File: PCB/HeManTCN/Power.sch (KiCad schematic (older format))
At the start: 10 parts

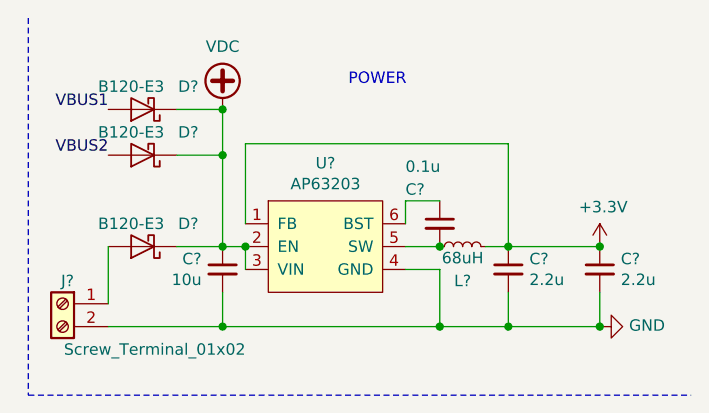
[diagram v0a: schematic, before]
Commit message: Hoja A1
Desarme las hojas jerarquicas y configure la hoja del esquematico como A1. Hay lugar suficiente (por ahora) para todo.
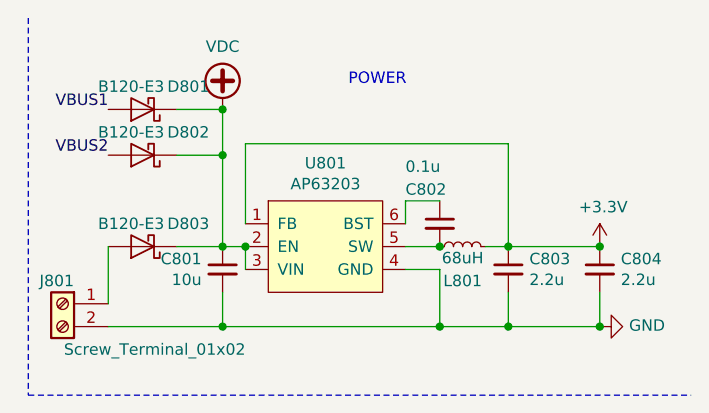
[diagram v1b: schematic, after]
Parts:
- gave numbers to parts that had none: 10
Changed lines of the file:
@@
 $Descr A4 11693 8268
 encoding utf-8
-Sheet 8 11
+Sheet 8 5
 Title "SnifferTCN"
 Date "2019-09-25"
@@
 U 1 1 5DA5E508
 P 6600 3850
-F 0 "C?" H 6692 3896 50  0000 L CNN
+AR Path="/5DA5E508" Ref="C?"  Part="1"
+AR Path="/5DA5E268/5DA5E508" Ref="C804"  Part="1"
+F 0 "C804" H 6692 3896 50  0000 L CNN
 F 1 "2.2u" H 6692 3805 50  0000 L CNN
 F 2 "Capacitor_SMD:C_0805_2012Metric" H 6600 3850 50  0001 C CNN
@@
 U 1 1 5DA5E510
 P 5900 3650
-F 0 "C?" H 5750 3800 50  0000 L CNN
+AR Path="/5DA5E510" Ref="C?"  Part="1"
+AR Path="/5DA5E268/5DA5E510" Ref="C802"  Part="1"
+F 0 "C802" H 5750 3800 50  0000 L CNN
 F 1 "0.1u" H 5750 3900 50  0000 L CNN
 F 2 "Capacitor_SMD:C_0805_2012Metric" H 5900 3650 50  0001 C CNN
@@
 U 1 1 5DA5E517
 P 6600 3750
-F 0 "#PWR?" H 6600 3600 50  0001 C CNN
+AR Path="/5DA5E517" Ref="#PWR?"  Part="1"
+AR Path="/5DA5E268/5DA5E517" Ref="#PWR0802"  Part="1"
+F 0 "#PWR0802" H 6600 3600 50  0001 C CNN
 F 1 "+3.3V" H 6615 3923 50  0000 C CNN
 F 2 "" H 6600 3750 50  0001 C CNN
@@
 U 1 1 5DA5E51D
 P 4950 3150
-F 0 "#PWR?" H 4950 3050 50  0001 C CNN
+AR Path="/5DA5E51D" Ref="#PWR?"  Part="1"
+AR Path="/5DA5E268/5DA5E51D" Ref="#PWR0801"  Part="1"
+F 0 "#PWR0801" H 4950 3050 50  0001 C CNN
 F 1 "VDC" H 4950 3425 50  0000 C CNN
 F 2 "" H 4950 3150 50  0001 C CNN
@@
 U 1 1 5DA5E523
 P 6600 4100
-F 0 "#PWR?" H 6600 3850 50  0001 C CNN
+AR Path="/5DA5E523" Ref="#PWR?"  Part="1"
+AR Path="/5DA5E268/5DA5E523" Ref="#PWR0803"  Part="1"
+F 0 "#PWR0803" H 6600 3850 50  0001 C CNN
 F 1 "GND" V 6605 3972 50  0000 R CNN
 F 2 "" H 6600 4100 50  0001 C CNN
@@
 U 1 1 5DA5E52A
 P 4250 4000
-F 0 "J?" H 4200 4100 50  0000 L CNN
+AR Path="/5DA5E52A" Ref="J?"  Part="1"
+AR Path="/5DA5E268/5DA5E52A" Ref="J801"  Part="1"
+F 0 "J801" H 4200 4100 50  0000 L CNN
 F 1 "Screw_Terminal_01x02" H 3450 3800 50  0000 L CNN
 F 2 "Connectors_Phoenix:PhoenixContact_MC-G_02x5.08mm_Angled" H 4250 4000 50  0001 C CNN
@@
 U 1 1 5DA5E532
 P 4600 3750
-F 0 "D?" H 4400 3650 50  0000 C CNN
+AR Path="/5DA5E532" Ref="D?"  Part="1"
+AR Path="/5DA5E268/5DA5E532" Ref="D803"  Part="1"
+F 0 "D803" H 4400 3650 50  0000 C CNN
 F 1 "B120-E3" H 4650 3650 50  0000 C CNN
 F 2 "Diode_SMD:D_SOD-123" H 4600 3575 50  0001 C CNN
@@
 U 1 1 5DA5E53D
 P 4600 3350
-F 0 "D?" H 4400 3250 50  0000 C CNN
+AR Path="/5DA5E53D" Ref="D?"  Part="1"
+AR Path="/5DA5E268/5DA5E53D" Ref="D802"  Part="1"
+F 0 "D802" H 4400 3250 50  0000 C CNN
 F 1 "B120-E3" H 4650 3250 50  0000 C CNN
 F 2 "Diode_SMD:D_SOD-123" H 4600 3175 50  0001 C CNN
@@
 U 1 1 5DA5E545
 P 4600 3150
-F 0 "D?" H 4400 3050 50  0000 C CNN
+AR Path="/5DA5E545" Ref="D?"  Part="1"
+AR Path="/5DA5E268/5DA5E545" Ref="D801"  Part="1"
+F 0 "D801" H 4400 3050 50  0000 C CNN
 F 1 "B120-E3" H 4650 3050 50  0000 C CNN
 F 2 "Diode_SMD:D_SOD-123" H 4600 2975 50  0001 C CNN
@@
 U 1 1 5DA5E552
 P 5400 3750
-F 0 "U?" H 5400 4115 50  0000 C CNN
+AR Path="/5DA5E552" Ref="U?"  Part="1"
+AR Path="/5DA5E268/5DA5E552" Ref="U801"  Part="1"
+F 0 "U801" H 5400 4115 50  0000 C CNN
 F 1 "AP63203" H 5400 4024 50  0000 C CNN
 F 2 "Package_TO_SOT_SMD:TSOT-23-6" H 5400 3750 50  0001 C CNN
@@
 U 1 1 5DA5E55A
 P 6200 3850
-F 0 "C?" H 6292 3896 50  0000 L CNN
+AR Path="/5DA5E55A" Ref="C?"  Part="1"
+AR Path="/5DA5E268/5DA5E55A" Ref="C803"  Part="1"
+F 0 "C803" H 6292 3896 50  0000 L CNN
 F 1 "2.2u" H 6292 3805 50  0000 L CNN
 F 2 "Capacitor_SMD:C_0805_2012Metric" H 6200 3850 50  0001 C CNN
@@
 U 1 1 5DA5E562
 P 6000 3750
-F 0 "L?" V 5850 3750 50  0000 C CNN
+AR Path="/5DA5E562" Ref="L?"  Part="1"
+AR Path="/5DA5E268/5DA5E562" Ref="L801"  Part="1"
+F 0 "L801" V 5850 3750 50  0000 C CNN
 F 1 "68uH" V 5950 3750 50  0000 C CNN
 F 2 "Inductor_SMD:L_6.3x6.3_H3" H 6000 3750 50  0001 C CNN
@@
 U 1 1 5DA5E57C
 P 4950 3850
-F 0 "C?" H 4858 3896 50  0000 R CNN
+AR Path="/5DA5E57C" Ref="C?"  Part="1"
+AR Path="/5DA5E268/5DA5E57C" Ref="C801"  Part="1"
+F 0 "C801" H 4858 3896 50  0000 R CNN
 F 1 "10u" H 4858 3805 50  0000 R CNN
 F 2 "Capacitor_SMD:C_0805_2012Metric" H 4950 3850 50  0001 C CNN
